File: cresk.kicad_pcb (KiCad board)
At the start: 2 copper layers, 116 x 80.2 mm, 38 parts, among them J1 8P8C, J2 8P8C, SW1 SW_PUSH, SW10 SW_PUSH, SW11 SW_PUSH, SW12 SW_PUSH, SW13 SW_PUSH, SW14 SW_PUSH, SW15 SW_PUSH, SW16 SW_PUSH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

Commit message: feat(pcb): reposition row3 diodes
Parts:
- moved D14 12.0 mm to (151.0, 44.0), turned to 180 degrees
- moved D15 10.8 mm to (151.0, 63.0), turned to 180 degrees
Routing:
- net col1: track 223.4 -> 213.6 mm
- net row3: track 45.4 -> 41.2 mm
- net col2: track 217.8 -> 214.2 mm
- net row0: track 101.7 -> 99.4 mm
- net col0: track 251.1 -> 249.6 mm
- net Net-(D15-Pad2): track 10.3 -> 9.19 mm
- net VCC: track 9.94 -> 9.20 mm
- net Net-(D14-Pad2): track 9.80 -> 9.19 mm

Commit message: feat: add name
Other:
- board text added: "cresk"
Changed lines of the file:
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@@
   (gr_line (start 168.41 34.54) (end 157.77 34.54) (layer "Edge.Cuts") (width 0.1))
   (gr_line (start 168.41 24.34) (end 168.41 34.54) (layer "Edge.Cuts") (width 0.1))
+  (gr_text "cresk\n " (at 79.27 86.57) (layer "F.SilkS")
+    (effects (font (size 1 1) (thickness 0.15)) (justify left))
+  )
   (segment (start 155.47 49.74) (end 151.66 49.74) (width 0.381) (layer "F.Cu") (net 1))
   (segment (start 142.71 40.79) (end 137.75 40.79) (width 0.381) (layer "F.Cu") (net 1))

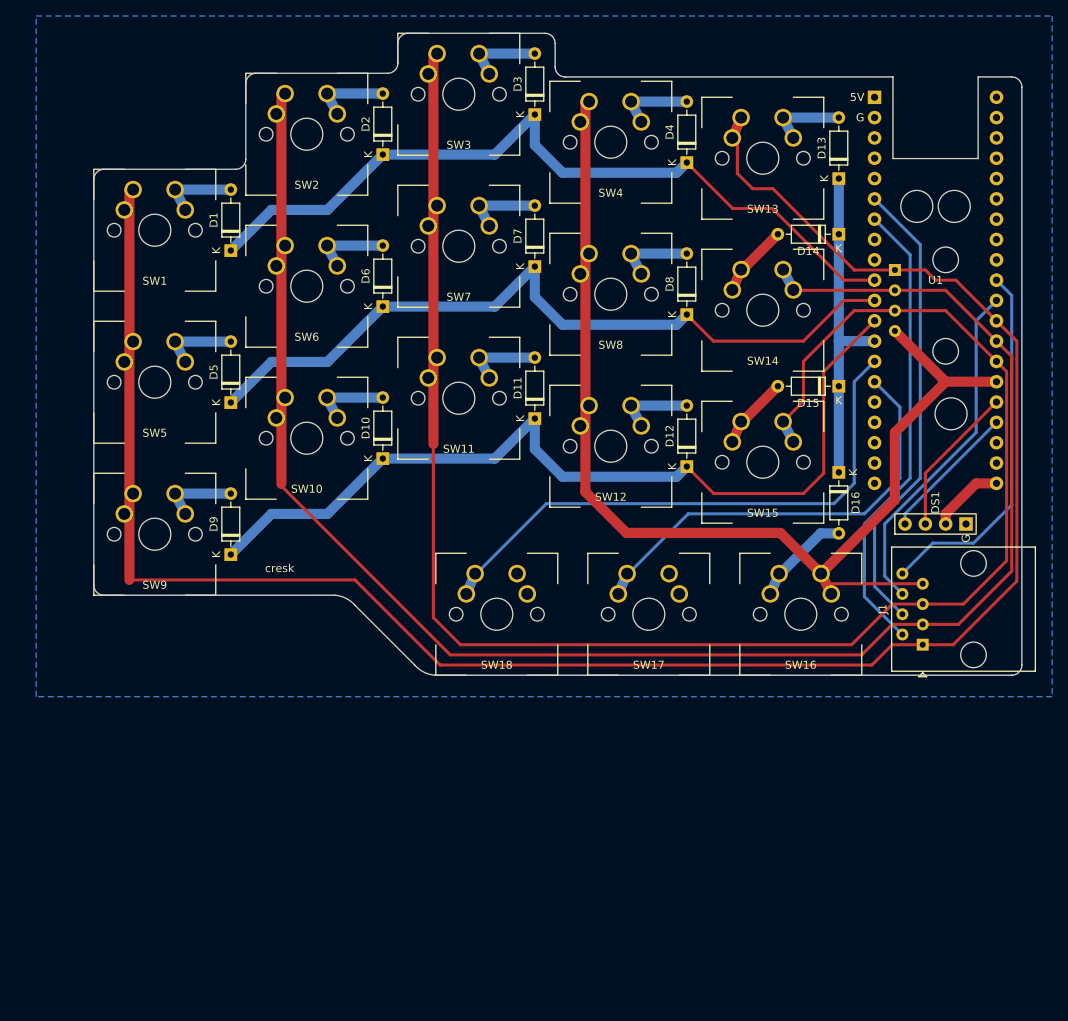
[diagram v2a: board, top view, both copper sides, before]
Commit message: feat: replace cresk with cresk v2
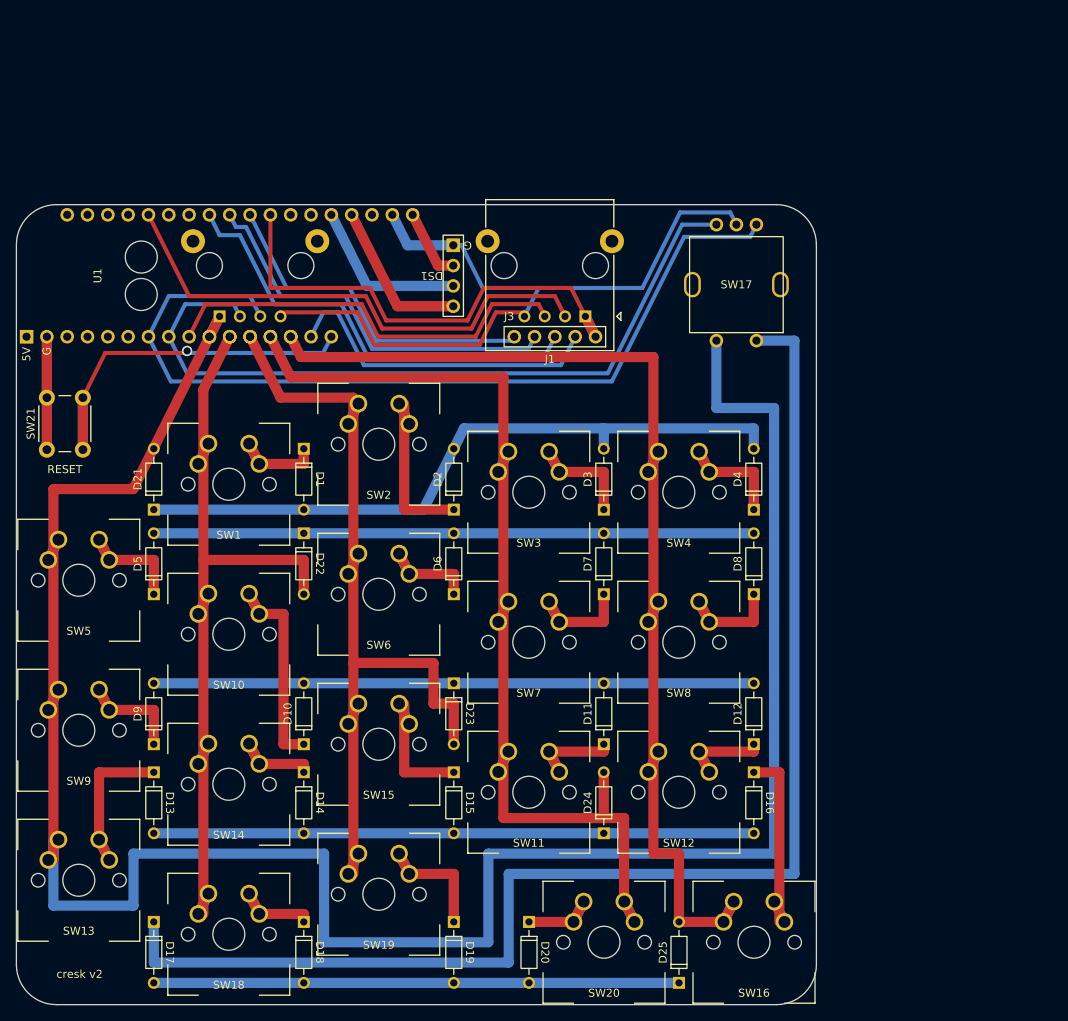
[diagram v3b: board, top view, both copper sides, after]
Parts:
- added D17: 1N4148, cresk:D_DO-35, F.Cu at (65.4, 130.0)
- added D18: 1N4148, cresk:D_DO-35, F.Cu at (84.1, 130.0)
- added D19: 1N4148, cresk:D_DO-35, F.Cu at (102.9, 130.0)
- added D20: 1N4148, cresk:D_DO-35, F.Cu at (112.3, 130.0)
- added D21: 1N4148, cresk:D_DO-35, F.Cu at (65.4, 78.4)
- added D22: 1N4148, cresk:D_DO-35, F.Cu at (84.1, 81.4)
- added D23: 1N4148, cresk:D_DO-35, F.Cu at (102.9, 100.1)
- added D24: 1N4148, cresk:D_DO-35, F.Cu at (121.6, 118.9)
- added D25: 1N4148, cresk:D_DO-35, F.Cu at (131.0, 137.6)
- added J3: Conn_01x05_Male, cresk:J-01x05, F.Cu at (120.6, 56.8)
- added J4: Conn_01x05_Male, cresk:J-01x05, B.Cu at (72.3, 56.8)
- added SW19: SW_Push, cresk:SW_MX_1u_Reversible, F.Cu at (93.5, 126.5)
- added SW20: SW_Push, cresk:SW_MX_1u_Reversible, F.Cu at (121.7, 132.5)
- added SW21: SW_Push, Button_Switch_THT:SW_PUSH_6mm, F.Cu at (52.0, 70.9)
- D1, D10, D11, D12, D13, D14, D15, D16, D2, D3, D4, D5, D6, D7, D8, D9: footprint Diode_THT:D_DO-35_SOD27_P7.62mm_Horizontal -> cresk:D_DO-35
- J1, J2: footprint Connector_RJ:RJ45_Amphenol_54602-x08_Horizontal -> Connector_RJ:RJ45_Ninigi_GE
- SW1, SW10, SW11, SW12, SW13, SW14, SW15, SW16, SW18, SW2, SW3, SW4, SW5, SW6, SW7, SW8, SW9: value SW_PUSH -> SW_Push
- SW17: value SW_PUSH -> EC11; footprint cresk:SW_MX_1u_Reversible -> cresk:EC11
- moved SW13 124.3 mm to (56.0, 124.8)
- moved D13 113.3 mm to (65.4, 111.3), turned to -90 degrees
- moved U1 110.1 mm to (49.5, 56.8), turned to 90 degrees
- moved D14 94.8 mm to (84.1, 111.3), turned to -90 degrees
- moved SW14 89.3 mm to (74.8, 112.8)
- moved J2 84.6 mm to (73.6, 54.3), turned to 0 degrees
- moved DS1 72.9 mm to (102.8, 45.4), turned to 180 degrees
- moved D15 68.2 mm to (102.9, 111.3), turned to -90 degrees
- moved SW15 59.6 mm to (93.5, 107.8)
- moved J1 58.8 mm to (119.3, 54.3), turned to 180 degrees
- moved SW18 52.2 mm to (74.8, 131.5)
- moved SW3 50.5 mm to (112.2, 76.2)
- moved SW7 50.3 mm to (112.2, 95.0)
- moved D3 50.1 mm to (121.6, 78.4)
- moved SW11 50.0 mm to (112.2, 113.8)
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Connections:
- net row6 renamed col6
- D1 pad 1: row0 -> Net-(D1-Pad1)
- D1 pad 2: Net-(D1-Pad2) -> row0
- D10 pad 1: row2 -> Net-(D10-Pad1)
- D10 pad 2: Net-(D10-Pad2) -> row2
- D11 pad 1: row2 -> Net-(D11-Pad1)
- D11 pad 2: Net-(D11-Pad2) -> row2
- D12 pad 1: row2 -> Net-(D12-Pad1)
- D12 pad 2: Net-(D12-Pad2) -> row2
- D13 pad 1: row3 -> Net-(D13-Pad1)
- D13 pad 2: Net-(D13-Pad2) -> row3
- D14 pad 1: row3 -> Net-(D14-Pad1)
- D14 pad 2: Net-(D14-Pad2) -> row3
- D15 pad 1: row3 -> Net-(D15-Pad1)
- D15 pad 2: Net-(D15-Pad2) -> row3
- D16 pad 1: row3 -> Net-(D16-Pad1)
- D16 pad 2: Net-(D16-Pad2) -> row3
- D2 pad 1: row0 -> Net-(D2-Pad1)
- D2 pad 2: Net-(D2-Pad2) -> row0
- D3 pad 1: row0 -> Net-(D3-Pad1)
- D3 pad 2: Net-(D3-Pad2) -> row0
- D4 pad 1: row0 -> Net-(D4-Pad1)
- D4 pad 2: Net-(D4-Pad2) -> row0
- D5 pad 1: row1 -> Net-(D5-Pad1)
- D5 pad 2: Net-(D5-Pad2) -> row1
- D6 pad 1: row1 -> Net-(D6-Pad1)
- D6 pad 2: Net-(D6-Pad2) -> row1
- D7 pad 1: row1 -> Net-(D7-Pad1)
- D7 pad 2: Net-(D7-Pad2) -> row1
- D8 pad 1: row1 -> Net-(D8-Pad1)
- D8 pad 2: Net-(D8-Pad2) -> row1
- D9 pad 1: row2 -> Net-(D9-Pad1)
- D9 pad 2: Net-(D9-Pad2) -> row2
- J1 pad 1: col0 -> col9
- J1 pad 2: row4 -> col8
- J1 pad 3: col1 -> b2
- J1 pad 4: row5 -> col7
- J1 pad 5: col2 -> a2
- J1 pad 7: col3 -> GND
- J1 pad 8: row7 -> col5
- J2 pad 2: row0 -> col1
- J2 pad 3: col1 -> b1
- J2 pad 4: row1 -> col2
- J2 pad 5: col2 -> a1
- J2 pad 6: row2 -> col3
- J2 pad 7: col3 -> GND
- J2 pad 8: row3 -> col4
- SW1 pad 1: col0 -> col1
- SW1 pad 2: Net-(D1-Pad2) -> Net-(D1-Pad1)
- SW10 pad 2: Net-(D10-Pad2) -> Net-(D10-Pad1)
- SW11 pad 1: col2 -> col3
- SW11 pad 2: Net-(D11-Pad2) -> Net-(D11-Pad1)
- SW12 pad 1: col3 -> col4
- SW12 pad 2: Net-(D12-Pad2) -> Net-(D12-Pad1)
- SW13 pad 2: Net-(D13-Pad2) -> Net-(D13-Pad1)
- SW14 pad 2: Net-(D14-Pad2) -> Net-(D14-Pad1)
- SW15 pad 2: Net-(D15-Pad2) -> Net-(D15-Pad1)
- SW16 pad 1: col3 -> col4
- SW16 pad 2: Net-(D16-Pad2) -> Net-(D16-Pad1)
- SW17 pad 1: col4 -> a1
- SW18 pad 1: col5 -> col1
- SW18 pad 2: GND -> Net-(D18-Pad1)
- SW2 pad 1: col1 -> col2
- SW2 pad 2: Net-(D2-Pad2) -> Net-(D2-Pad1)
- SW3 pad 1: col2 -> col3
- SW3 pad 2: Net-(D3-Pad2) -> Net-(D3-Pad1)
- SW4 pad 1: col3 -> col4
- SW4 pad 2: Net-(D4-Pad2) -> Net-(D4-Pad1)
- SW5 pad 2: Net-(D5-Pad2) -> Net-(D5-Pad1)
- SW6 pad 1: col1 -> col2
- SW6 pad 2: Net-(D6-Pad2) -> Net-(D6-Pad1)
- SW7 pad 1: col2 -> col3
- SW7 pad 2: Net-(D7-Pad2) -> Net-(D7-Pad1)
- SW8 pad 1: col3 -> col4
- SW8 pad 2: Net-(D8-Pad2) -> Net-(D8-Pad1)
- SW9 pad 2: Net-(D9-Pad2) -> Net-(D9-Pad1)
- U1 pad 10: row0 -> col0
- U1 pad 11: row1 -> col1
- U1 pad 12: row2 -> col2
- U1 pad 13: row3 -> col3
- U1 pad 14: col5 -> col4
- U1 pad 15: col4 -> col8
- U1 pad 16: unconnected-(U1-Pad16) -> Net-(SW21-Pad2)
- U1 pad 26: col3 -> unconnected-(U1-Pad26)
- U1 pad 27: col2 -> unconnected-(U1-Pad27)
- U1 pad 28: col1 -> col9
- U1 pad 29: col0 -> col5
- U1 pad 31: row7 -> col7
- U1 pad 34: unconnected-(U1-Pad34) -> b2
- U1 pad 6: row5 -> unconnected-(U1-Pad6)
- U1 pad 7: row4 -> a1
- U1 pad 8: unconnected-(U1-Pad8) -> b1
- U1 pad 9: unconnected-(U1-Pad9) -> a2
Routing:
- net p1: track 0.00 -> 167.7 mm
- net GND: track 0.00 -> 123.2 mm
- net col1: track 213.6 -> 101.1 mm
- net a1: track 0.00 -> 110.2 mm
- net col2: track 214.2 -> 111.2 mm
- net b1: track 0.00 -> 95.1 mm
- net col4: track 55.0 -> 140.5 mm
- net b2: track 0.00 -> 64.9 mm
- net col9: track 0.00 -> 61.4 mm
- net row5: track 58.1 -> 0.00 mm
- net col7: track 0.00 -> 55.7 mm
- net a2: track 0.00 -> 52.9 mm
- net Net-(SW21-Pad2): track 0.00 -> 48.5 mm, vias 0 -> 1
- net row7: track 46.1 -> 0.00 mm
- net col8: track 0.00 -> 41.2 mm
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- removed copper zone on B.Cu, net GND
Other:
- board size 116 x 80.2 mm -> 100 x 100 mm
- board text added: "RESET"
- board text added: "cresk v2"
- board text removed: "cresk"
